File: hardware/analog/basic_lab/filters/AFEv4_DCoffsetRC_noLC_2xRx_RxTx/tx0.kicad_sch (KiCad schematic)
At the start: 1 part

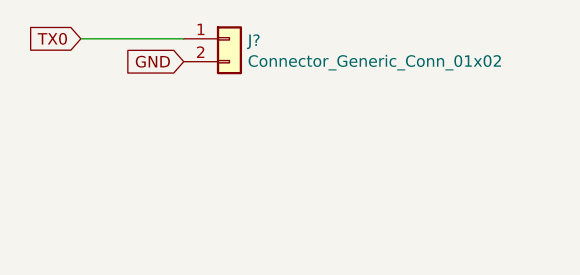
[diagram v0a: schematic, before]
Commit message: started 2xRx / RxTx PCBs with no / simple LC filters
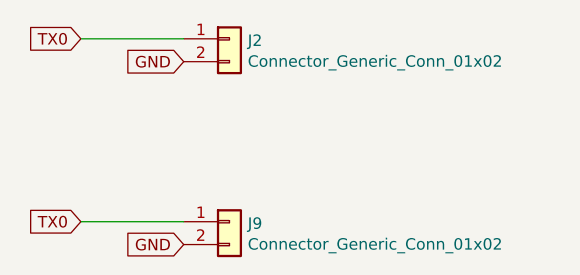
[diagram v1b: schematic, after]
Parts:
- added J9: Connector_Generic_Conn_01x02, Connector_PinHeader_2.54mm:PinHeader_1x02_P2.54mm_Vertical, symbol bgt:Connector_Generic_Conn_01x02
- gave numbers to parts that had none: 1
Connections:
- net GND: now also J9.2 (Pin_2)
- net TX0: now also J9.1 (Pin_1)
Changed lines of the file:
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@@
     (stroke (width 0) (type default) (color 0 0 0 0))
+  )
+  (wire (pts (xy 83.82 90.17) (xy 95.25 90.17))
+    (stroke (width 0) (type default) (color 0 0 0 0))
+  )
+  (global_label "TX0" (shape input) (at 83.82 90.17 180) (fields_autoplaced)
+    (effects (font (size 1.27 1.27)) (justify right))
+    (property "Intersheet References" "${INTERSHEET_REFS}" (id 0) (at 78.1091 90.0906 0)
+      (effects (font (size 1.27 1.27)) (justify right) hide)
+    )
+  )
+  (global_label "GND" (shape input) (at 95.25 92.71 180) (fields_autoplaced)
+    (effects (font (size 1.27 1.27)) (justify right))
+    (property "Intersheet References" "${INTERSHEET_REFS}" (id 0) (at -35.56 34.29 0)
+      (effects (font (size 1.27 1.27)) hide)
+    )
   )
   (global_label "GND" (shape input) (at 95.25 72.39 180) (fields_autoplaced)
@@
   (symbol (lib_id "bgt:Connector_Generic_Conn_01x02") (at 100.33 69.85 0) (unit 1)
     (in_bom yes) (on_board yes)
-    (property "Reference" "J?" (id 0) (at 102.362 70.0532 0)
+    (property "Reference" "J2" (id 0) (at 102.362 70.0532 0)
       (effects (font (size 1.27 1.27)) (justify left))
     )
@@
       (effects (font (size 1.27 1.27)) hide)
     )
+    (pin "1")
+    (pin "2")
+  )
+  (symbol (lib_id "bgt:Connector_Generic_Conn_01x02") (at 100.33 90.17 0) (unit 1)
+    (in_bom yes) (on_board yes)
+    (property "Reference" "J9" (id 0) (at 102.362 90.3732 0)
+      (effects (font (size 1.27 1.27)) (justify left))
+    )
+    (property "Value" "Connector_Generic_Conn_01x02" (id 1) (at 102.362 92.6846 0)
+      (effects (font (size 1.27 1.27)) (justify left))
+    )
+    (property "Footprint" "Connector_PinHeader_2.54mm:PinHeader_1x02_P2.54mm_Vertical" (id 2) (at 100.33 90.17 0)
+      (effects (font (size 1.27 1.27)) hide)
+    )
+    (property "Datasheet" "" (id 3) (at 100.33 90.17 0)
+      (effects (font (size 1.27 1.27)) hide)
+    )
